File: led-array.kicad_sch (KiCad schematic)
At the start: 38 parts, among them J1 USB_B_Micro, J2 Conn_01x04_Pin, Q1 Q_NMOS_GDS, Q2 Q_NMOS_GDS, Q3 Q_NMOS_GDS, Q4 Q_NMOS_GDS, Q5 Q_NMOS_GDS, Q6 Q_NMOS_GDS, Q7 Q_NMOS_GDS, Q8 Q_NMOS_GDS, U1 STM32F103C8T6, U4 TPS54331DR, Y1 16MHz

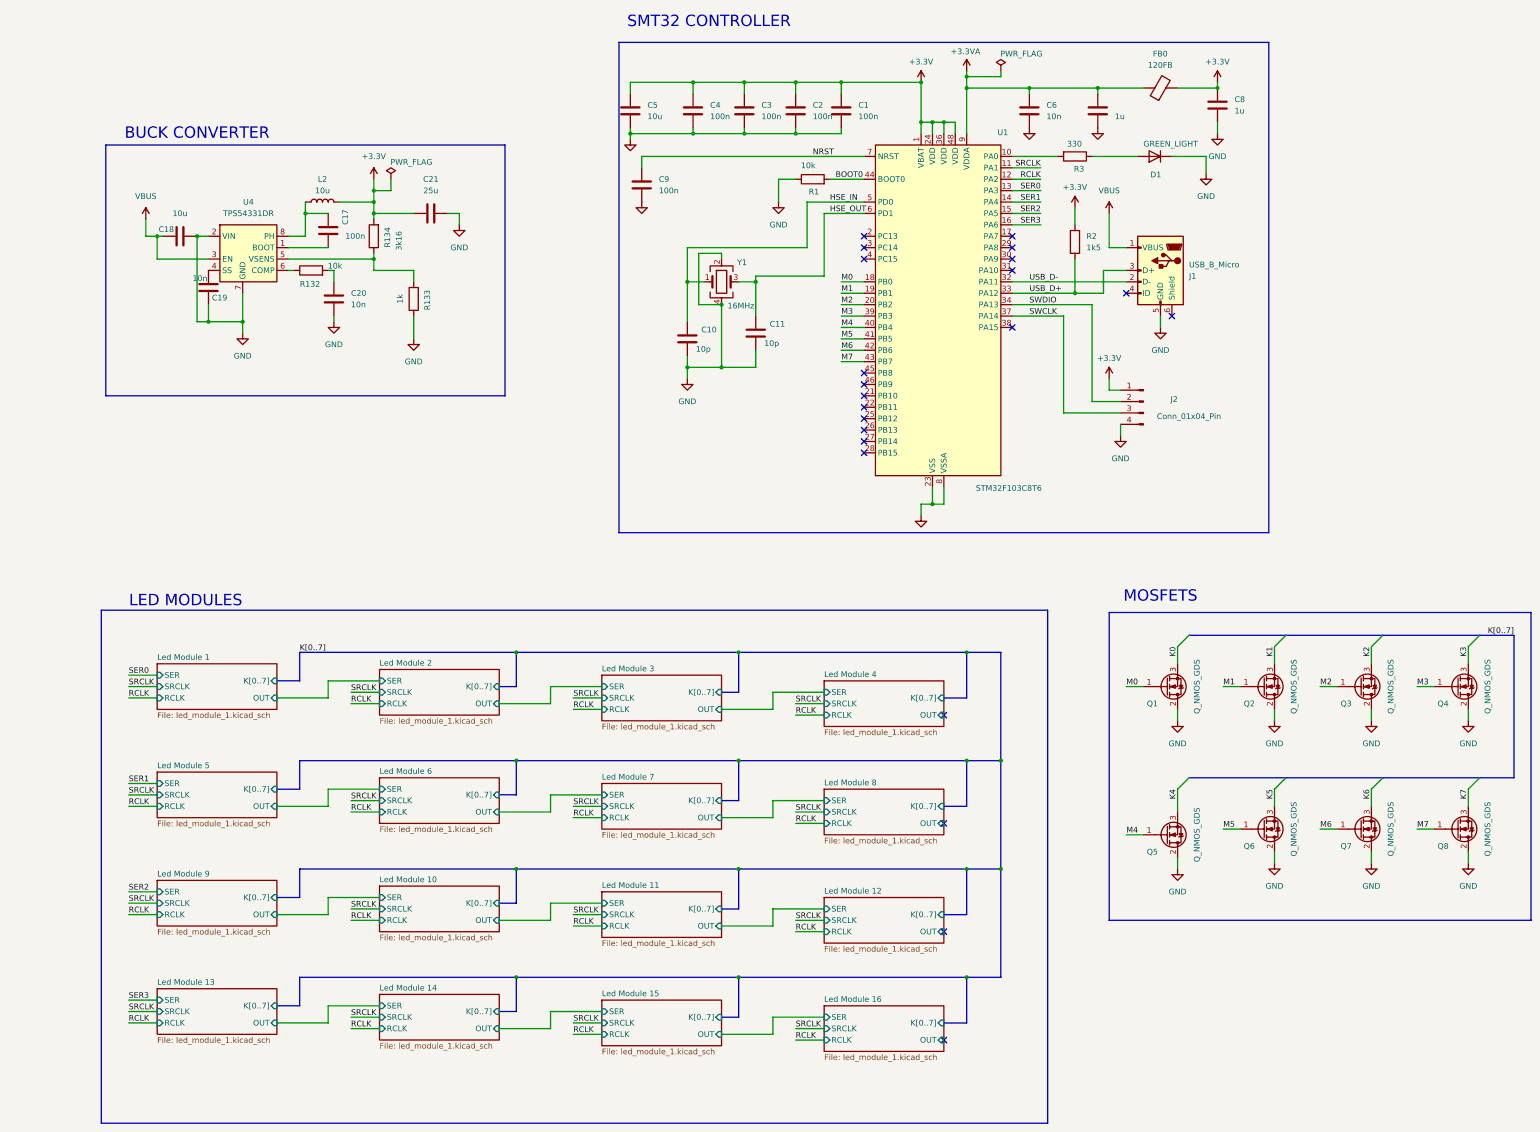
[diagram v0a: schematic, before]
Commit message: LED updates with some layout
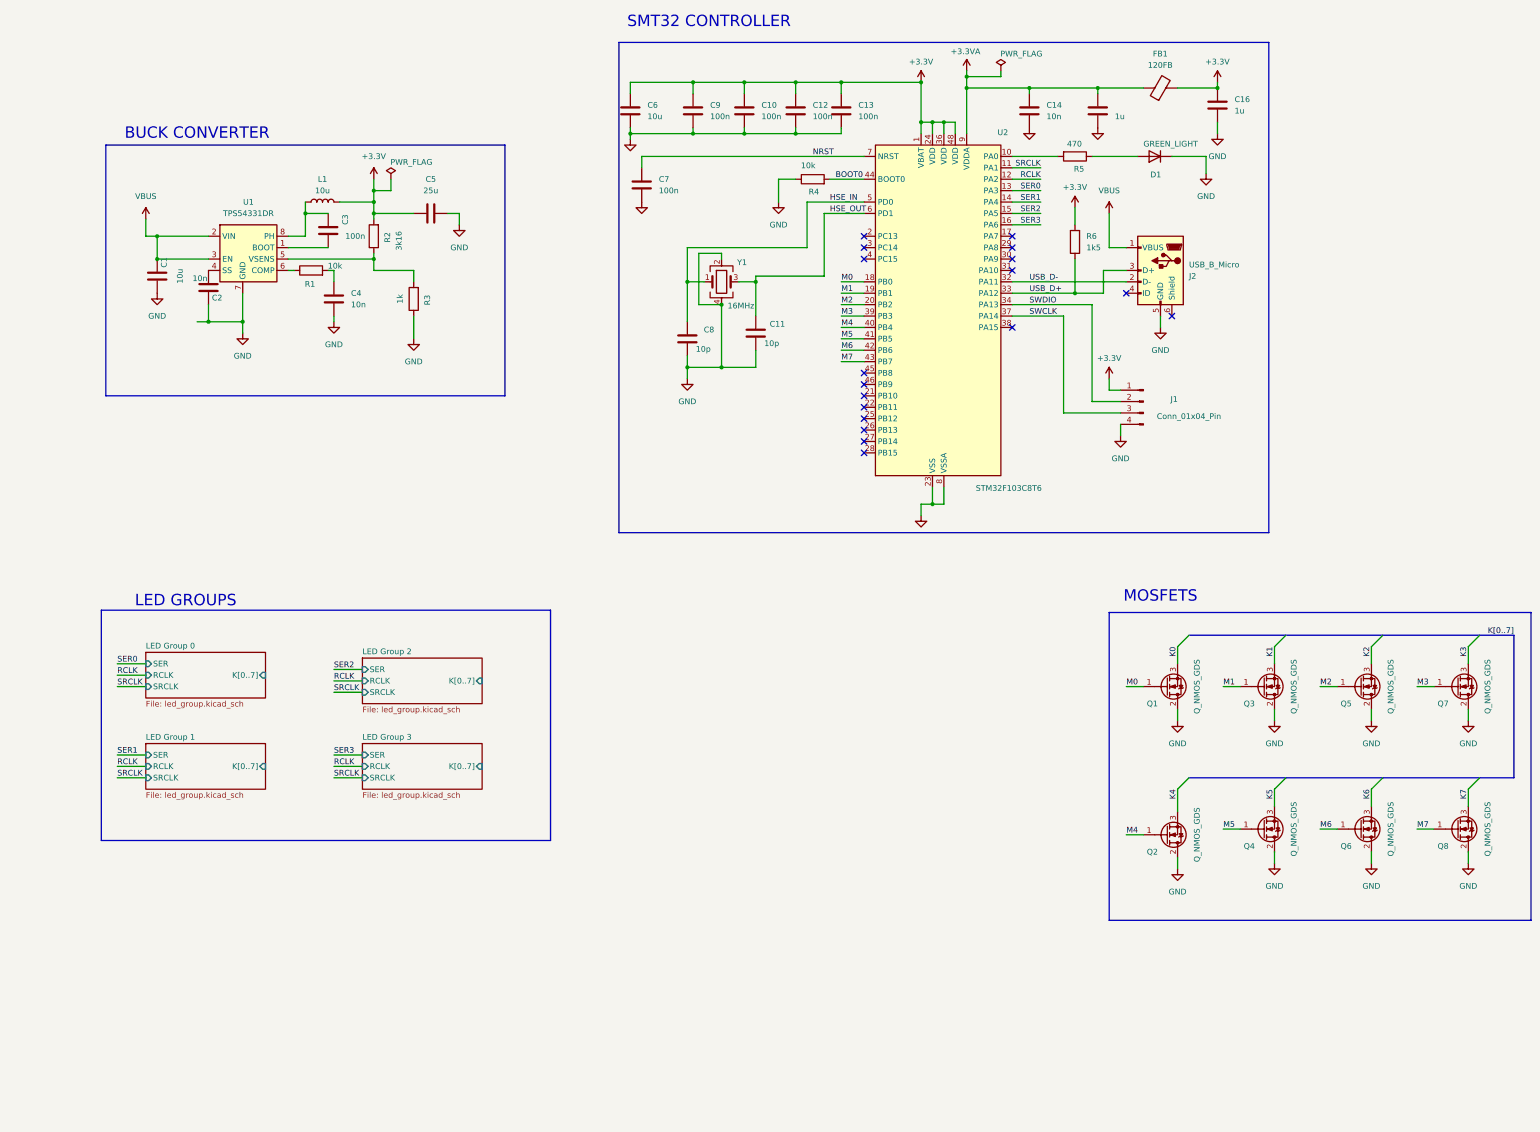
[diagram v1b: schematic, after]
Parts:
- removed C18: 10u, Capacitor_SMD:C_0603_1608Metric, symbol Device:C
- added C1: 10u, Capacitor_SMD:C_0603_1608Metric, symbol Device:C
- R5: renamed from R3; value 330 -> 470
- renumbered C3 to C10, C2 to C12, C1 to C13, C6 to C14, C7 to C15, C8 to C16, C19 to C2, C17 to C3, C20 to C4, C21 to C5, C5 to C6, C9 to C7, C10 to C8, C4 to C9, FB0 to FB1, J2 to J1, J1 to J2, L2 to L1, Q5 to Q2, Q2 to Q3, Q6 to Q4, Q3 to Q5, Q7 to Q6, Q4 to Q7, R132 to R1, R134 to R2, R133 to R3, R1 to R4, R2 to R6, U4 to U1, U1 to U2
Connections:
- net GND: now also C1.2; no longer U1.2 (VIN)
- net VBUS: now also U1.2 (VIN), C1.1
- no-connect marks 22 -> 18
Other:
- removed sheet Led Module 1
- removed sheet Led Module 10
- removed sheet Led Module 11
- removed sheet Led Module 12
- removed sheet Led Module 13
- removed sheet Led Module 14
- removed sheet Led Module 15
- removed sheet Led Module 16
- removed sheet Led Module 2
- removed sheet Led Module 3
- removed sheet Led Module 4
- removed sheet Led Module 5
- removed sheet Led Module 6
- removed sheet Led Module 7
- removed sheet Led Module 8
- removed sheet Led Module 9
- added sheet LED Group 0 (led_group.kicad_sch)
- added sheet LED Group 1 (led_group.kicad_sch)
- added sheet LED Group 2 (led_group.kicad_sch)
- added sheet LED Group 3 (led_group.kicad_sch)
- note added: "LED GROUPS"
- note removed: "LED MODULES"

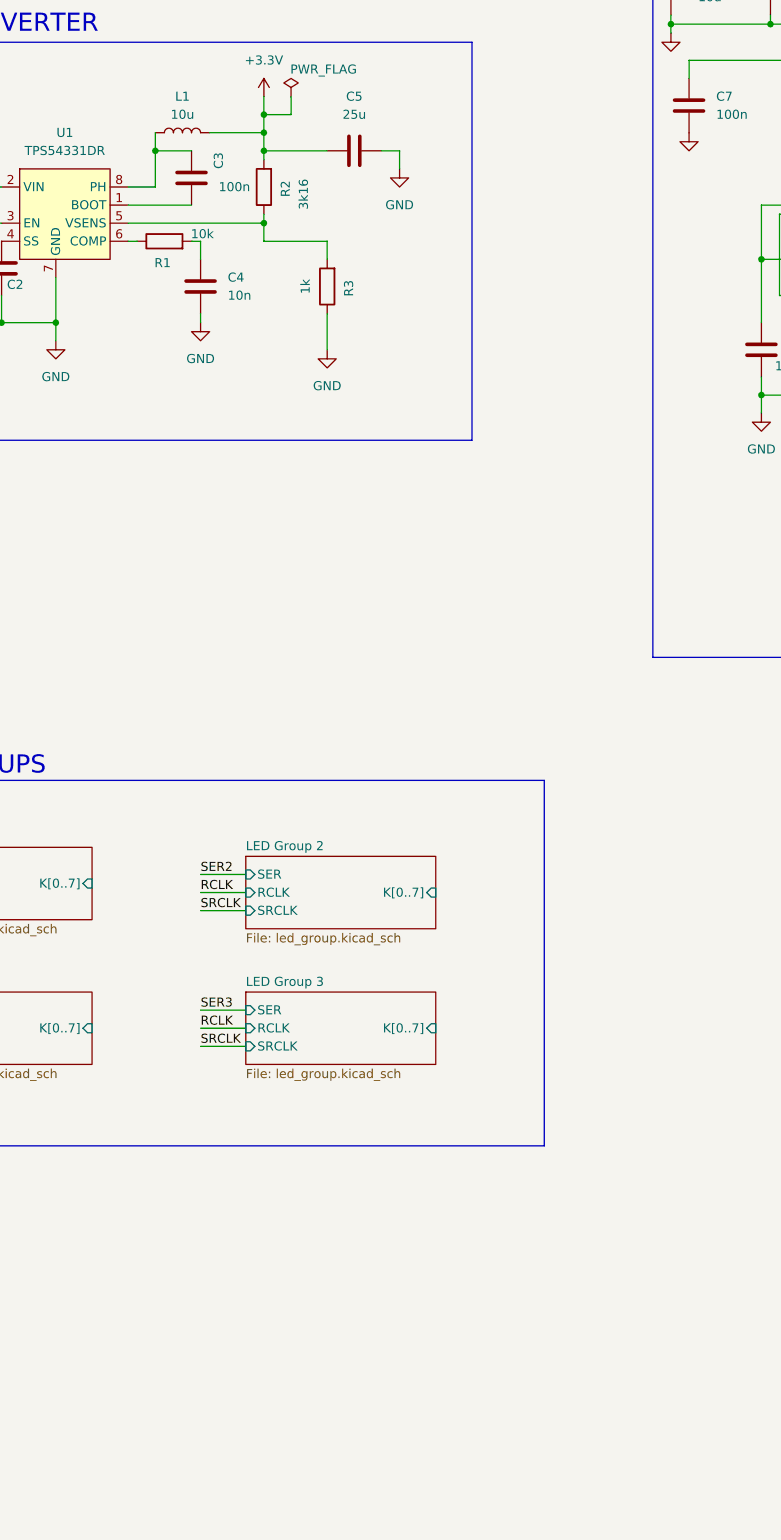
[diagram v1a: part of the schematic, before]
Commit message: LEDS wired
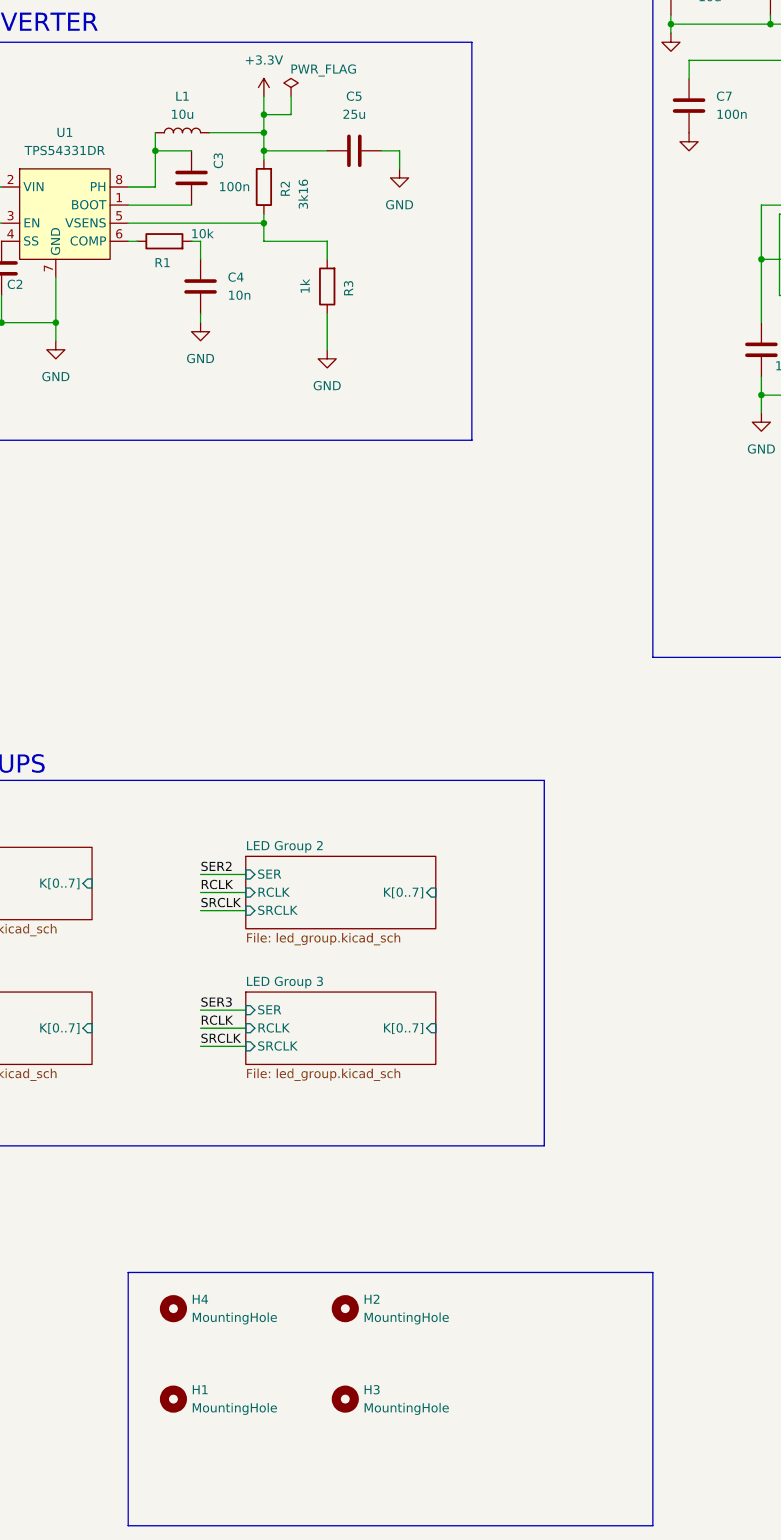
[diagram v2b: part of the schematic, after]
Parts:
- added H1, H2, H3, H4: MountingHole, MountingHole:MountingHole_3.2mm_M3, symbol Mechanical:MountingHole

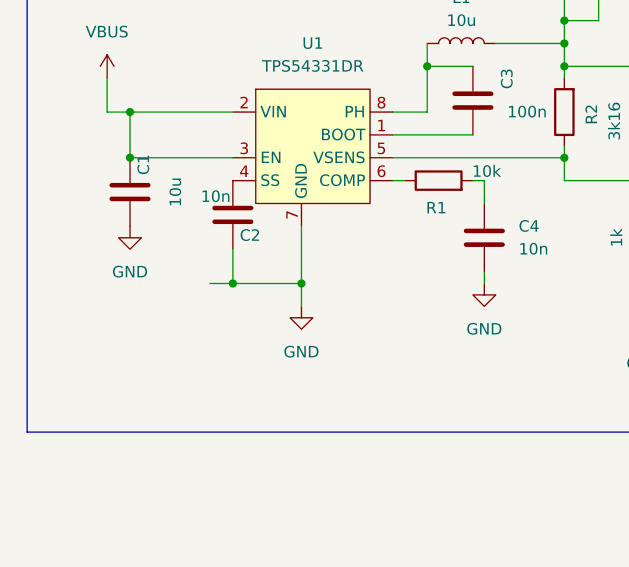
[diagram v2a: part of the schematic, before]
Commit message: Set up RCLK and SRCLK lines
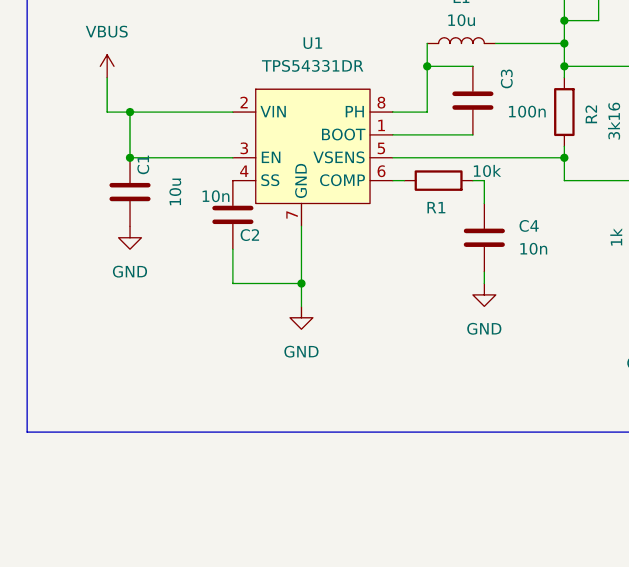
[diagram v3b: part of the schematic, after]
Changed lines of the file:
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@@
-	)
-	(junction
-		(at 43.18 92.71)
-		(diameter 0)
-		(color 0 0 0 0)
 	)
 	(junction
@@
 		)
 		(stroke
-			(width 0)
-			(type default)
-		)
-	)
-	(wire
-		(pts
-			(xy 40.64 92.71) (xy 43.18 92.71)
-		)
-		(stroke

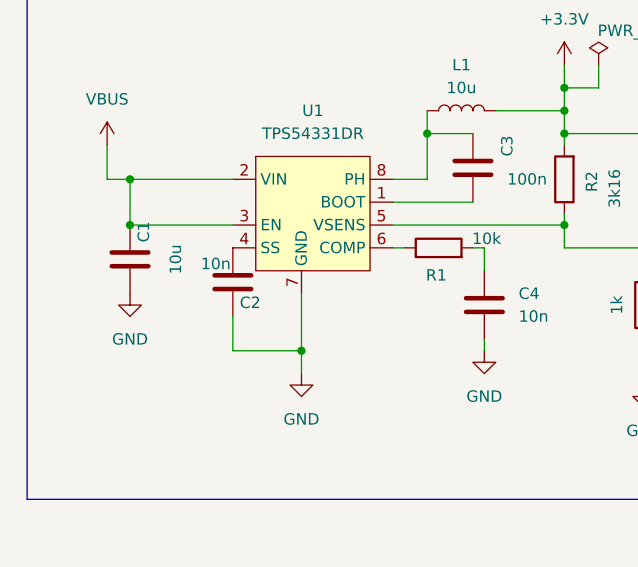
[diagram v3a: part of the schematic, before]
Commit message: Main power and signals wired
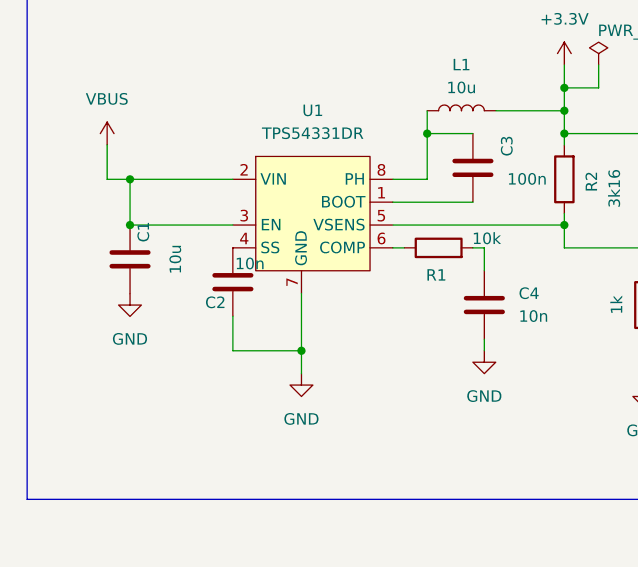
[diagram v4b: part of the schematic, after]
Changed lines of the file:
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@@
 		(lib_id "Device:C")
 		(at 43.18 85.09 0)
+		(mirror y)
 		(unit 1)
 		(exclude_from_sim no)
@@
 		(dnp no)
 		(property "Reference" "C2"
-			(at 43.942 87.376 0)
+			(at 42.418 87.376 0)
 			(effects
 				(font
@@
 		)
 		(property "Value" "10n"
-			(at 39.624 83.058 0)
+			(at 46.736 83.058 0)
 			(effects
 				(font
@@
 		)
 		(property "Footprint" "Capacitor_SMD:C_0402_1005Metric"
-			(at 44.1452 88.9 0)
+			(at 42.2148 88.9 0)
 			(effects
 				(font
